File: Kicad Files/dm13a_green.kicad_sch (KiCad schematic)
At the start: 21 parts, among them U5 DM13A-GREEN

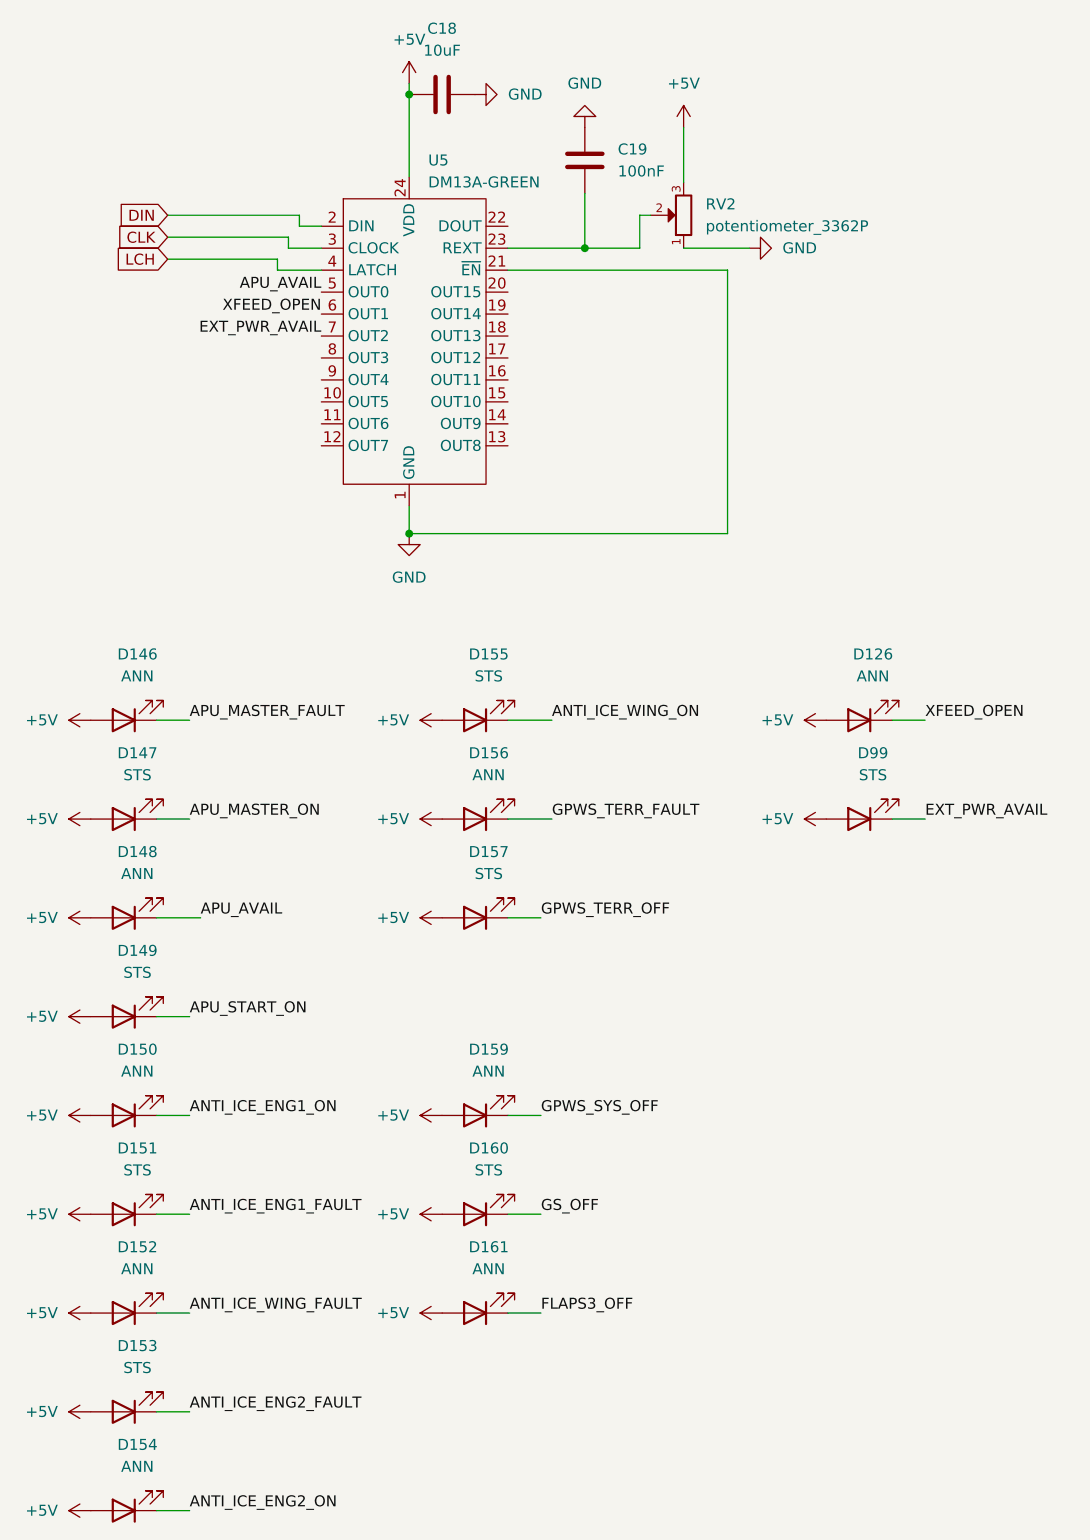
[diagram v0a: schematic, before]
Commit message: Keep the v1 project as KiCad recovered and saved it
KiCad recovered the board and it had to be saved, on top of edits made
to the project after the board was built. This commit keeps that state as
it is, so nothing is lost. It does not match the board that was fabricated.
The DRC finds the three ADIRS rotaries and NO SMOKING unconnected, and so
does every version committed since March 2025.

The next commit puts back the project as it was when the board was sent to
JLCPCB.

Co-Authored-By: Claude Opus 5.5 <noreply@anthropic.com>
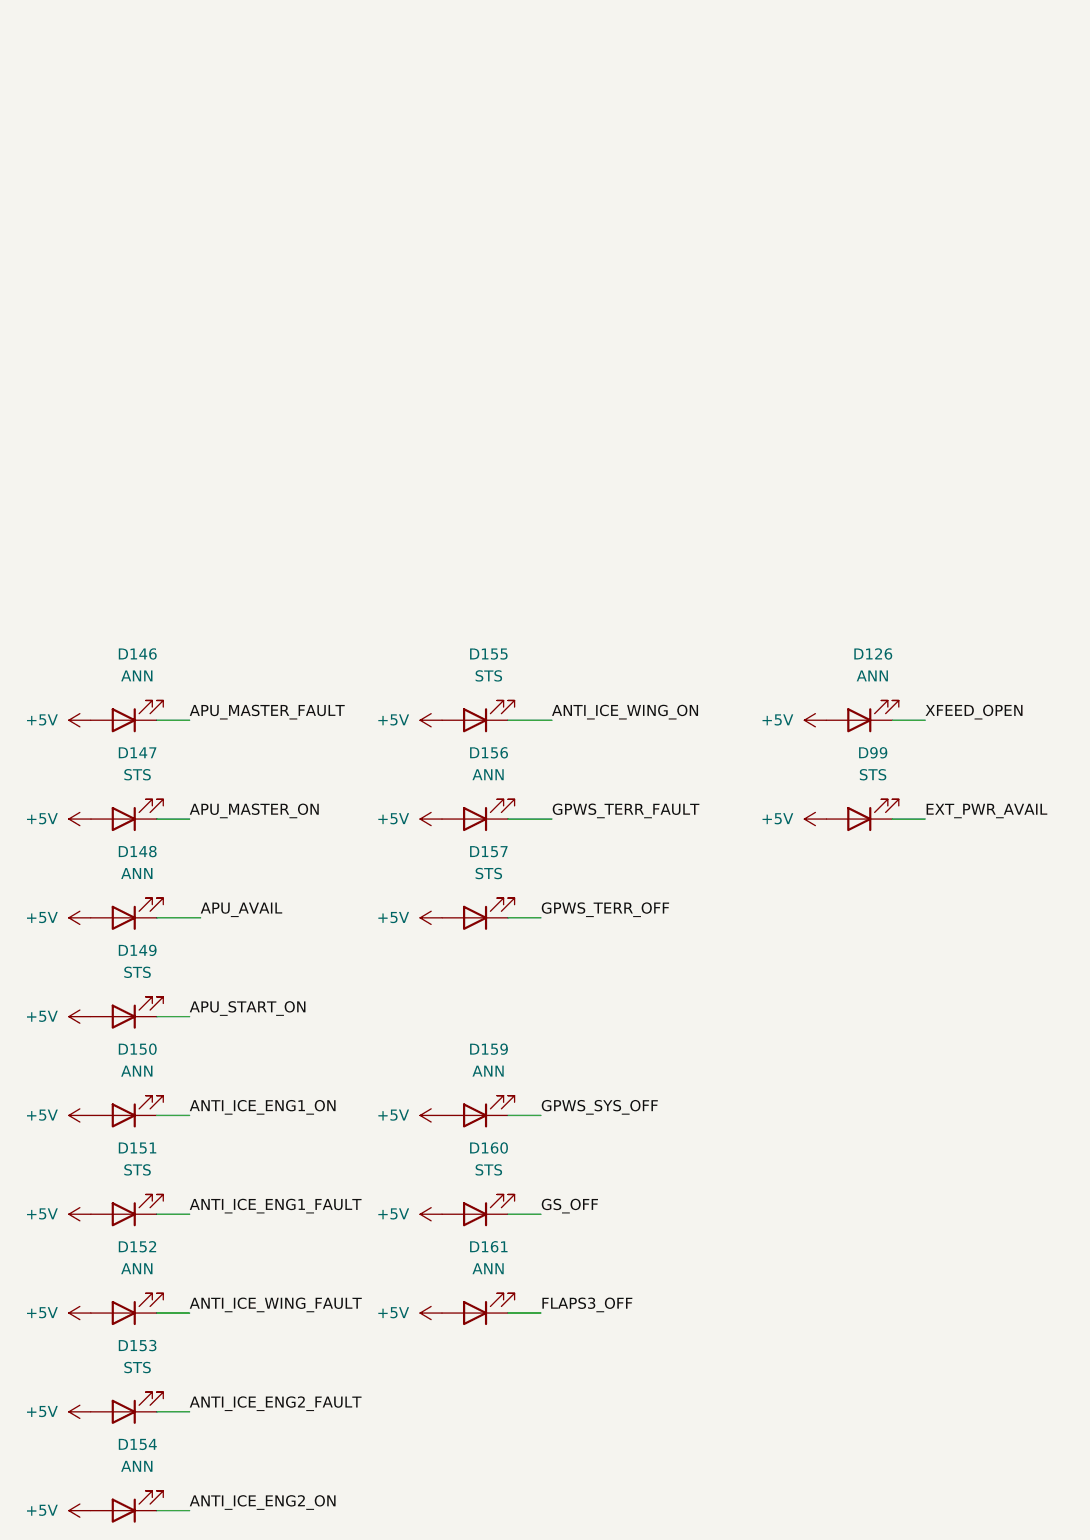
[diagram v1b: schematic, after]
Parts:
- removed C18: 10uF, Capacitor_SMD:C_1206_3216Metric_Pad1.33x1.80mm_HandSolder, symbol Device:C
- removed C19: 100nF, Capacitor_SMD:C_1206_3216Metric_Pad1.33x1.80mm_HandSolder, symbol Device:C
- removed RV2: potentiometer_3362P, PCM_SL_Footprints:potentiometer_3362P, symbol PCM_SL_Devices:potentiometer_3362P
- removed U5: DM13A-GREEN, Package_SO:SSOP-24_3.9x8.7mm_P0.635mm, symbol Custom_Symbols:DM13A

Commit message: Put back the v1 project as it was sent to JLCPCB, with the rotaries fixed
The board in the panel was ordered on 3 March 2025. The Gerbers uploaded to
JLCPCB for that order are byte-identical to production/OverHead_v1.zip,
exported that evening at 22:08. KiCad backed the project up at 22:06 and
at 22:26, with the same copper in both. This restores the 22:26 snapshot:
the board, the schematic sheets and the project files.

Its one flaw is in the file, not in the copper. On 22 February the three
ADIRS rotaries used SimPanel:Rotary_SW_8x1_SF, the footprint made for the
switches actually bought, whose pins sit one position round. By 3 March an
update from the schematic had put the library Rotary_SW_8x1 back under
the same tracks. The copper still reached the right physical pins, but the
file showed nine nets unconnected. The three footprints are taken back from
the 22 February board, with the same position, symbol link and nets. The
schematic now names _SF too, so the next update cannot undo it.

Checked on the result: the DRC finds 0 unconnected items. Following the
copper rather than the net names, each of the 49 buttons in the .mfmc
reaches exactly one switch contact, and each of the 44 annunciator outputs
reaches exactly one LED. The two "shorts" the DRC reports are copper the
schematic never drew: NO SMOKING's contact 3 on D5 and SEAT BELTS'
contact 3 on D18. The .mfmc reads NO SMOKING on D5, so the copper is what
works.

Co-Authored-By: Claude Opus 5.5 <noreply@anthropic.com>
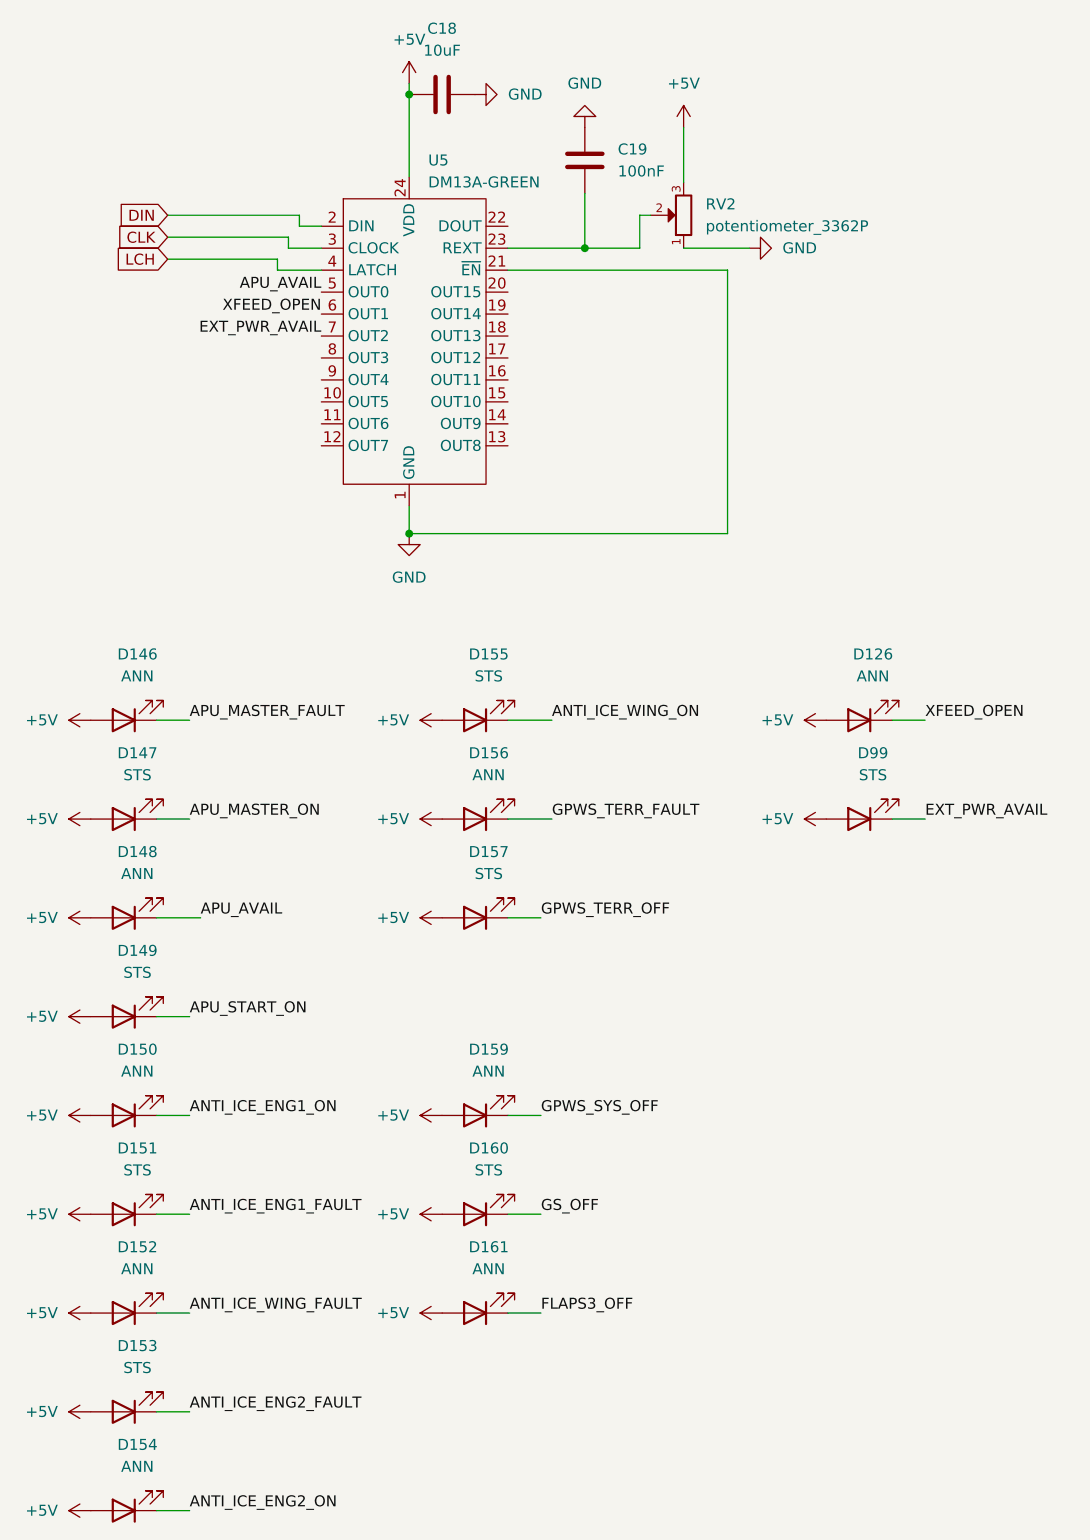
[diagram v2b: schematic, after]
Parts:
- added C18: 10uF, Capacitor_SMD:C_1206_3216Metric_Pad1.33x1.80mm_HandSolder, symbol Device:C
- added C19: 100nF, Capacitor_SMD:C_1206_3216Metric_Pad1.33x1.80mm_HandSolder, symbol Device:C
- added RV2: potentiometer_3362P, PCM_SL_Footprints:potentiometer_3362P, symbol PCM_SL_Devices:potentiometer_3362P
- added U5: DM13A-GREEN, Package_SO:SSOP-24_3.9x8.7mm_P0.635mm, symbol Custom_Symbols:DM13A
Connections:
- net +5V: now also C18.1, RV2.3, U5.24 (VDD)
- net APU_AVAIL: now also U5.5 (OUT0)
- net EXT_PWR_AVAIL: now also U5.7 (OUT2)
- net XFEED_OPEN: now also U5.6 (OUT1)
- new net: C19.2, RV2.2, U5.23 (REXT)
- new net CLK: U5.3 (CLOCK)
- new net DIN: U5.2 (DIN)
- new net GND: C18.2, C19.1, RV2.1, U5.1 (GND), U5.21 (~{EN})
- new net LCH: U5.4 (LATCH)
